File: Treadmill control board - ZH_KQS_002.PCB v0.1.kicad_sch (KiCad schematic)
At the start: 9 parts, among them Q1 IRG4PF50W

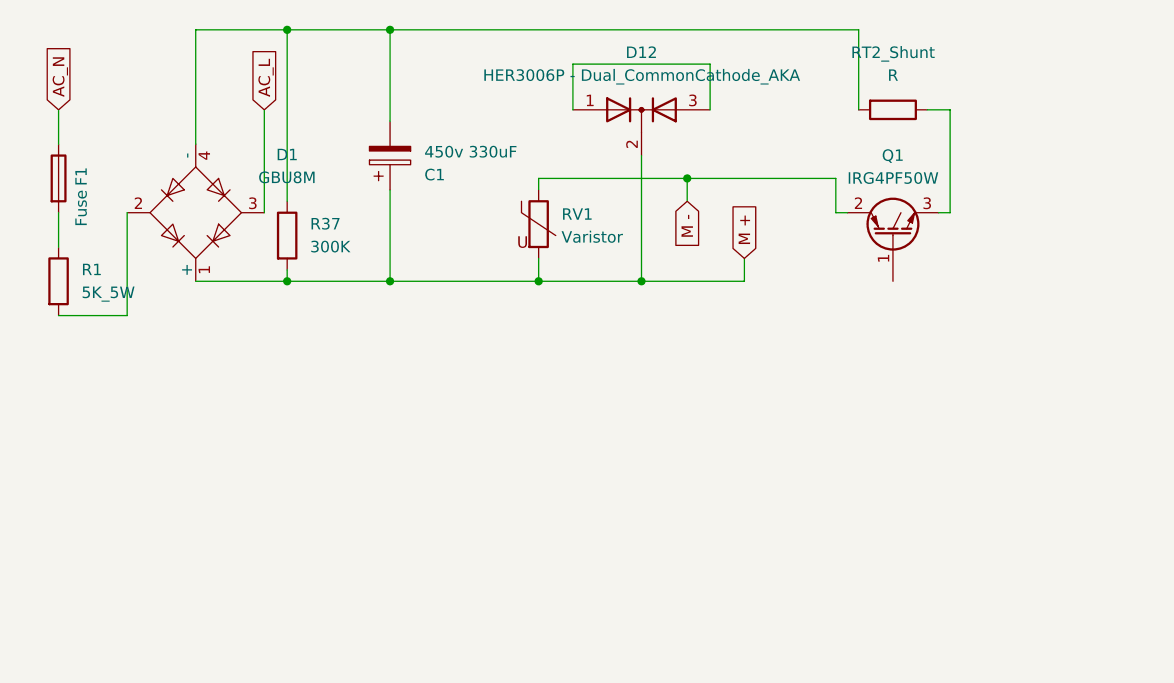
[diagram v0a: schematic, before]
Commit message: Schematic High Voltage side done
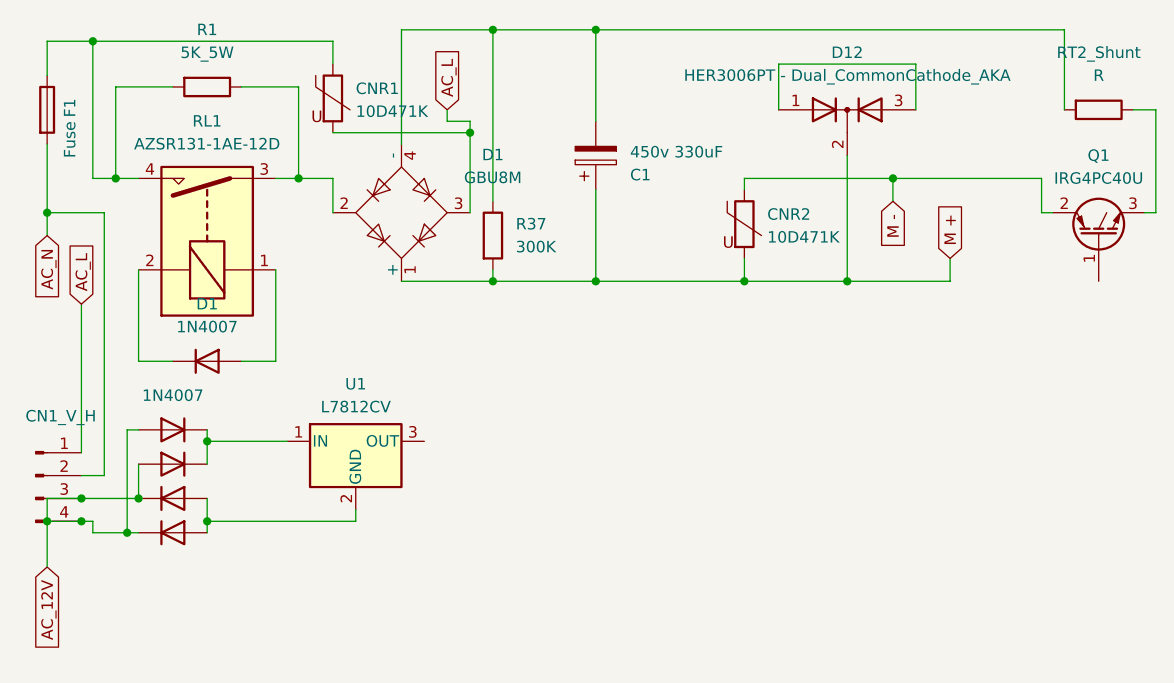
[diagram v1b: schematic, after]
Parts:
- added CN1_V_H: Conn_01x04_Pin, Connector_JST:JST_VH_B4P-VH_1x04_P3.96mm_Vertical, symbol Connector:Conn_01x04_Pin
- added CNR1: 10D471K, Varistor:RV_Disc_D21.5mm_W6.1mm_P7.5mm, symbol Device:Varistor
- added D1, D2, D3, D4, D5: 1N4007, Diode_THT:D_DO-41_SOD81_P10.16mm_Horizontal, symbol Diode:1N4007
- added RL1: AZSR131-1AE-12D, Relay_THT:Relay_SPST_Zettler-AZSR131, symbol Relay:AZSR131-1AE-12D
- added U1: L7812CV, Package_TO_SOT_THT:TO-220-3_Vertical, symbol Regulator_Linear:L7812
- CNR2: renamed from RV1; value Varistor -> 10D471K; footprint (none) -> Varistor:RV_Disc_D21.5mm_W6.1mm_P7.5mm
- D12: value HER3006P - Dual_CommonCathode_AKA -> HER3006PT - Dual_CommonCathode_AKA; footprint (none) -> Package_TO_SOT_THT:TO-247-3_Vertical
- Q1: value IRG4PF50W -> IRG4PC40U
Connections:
- net AC_L: now also CN1_V_H.1 (Pin_1), CNR1.2
- net AC_N: now also F1.2, CN1_V_H.2 (Pin_2); no longer F1.1
- net at R1.2: now also F1.1, CNR1.1, RL1.4; no longer D1.2
- net at R1.1: now also D1.2, RL1.3; no longer F1.2
- new net: D1.1 (K), RL1.2
- new net: D1.2 (A), RL1.1
- new net: D2.1 (K), D3.1 (K), U1.1 (IN)
- new net: D4.2 (A), D5.2 (A), U1.2 (GND)
- new net AC_12V: CN1_V_H.3 (Pin_3), CN1_V_H.4 (Pin_4), D2.2 (A), D3.2 (A), D4.1 (K), D5.1 (K)
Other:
- moved on the sheet: C1, CNR2, D1, D12, F1, Q1, R1, R37, RT2_Shunt

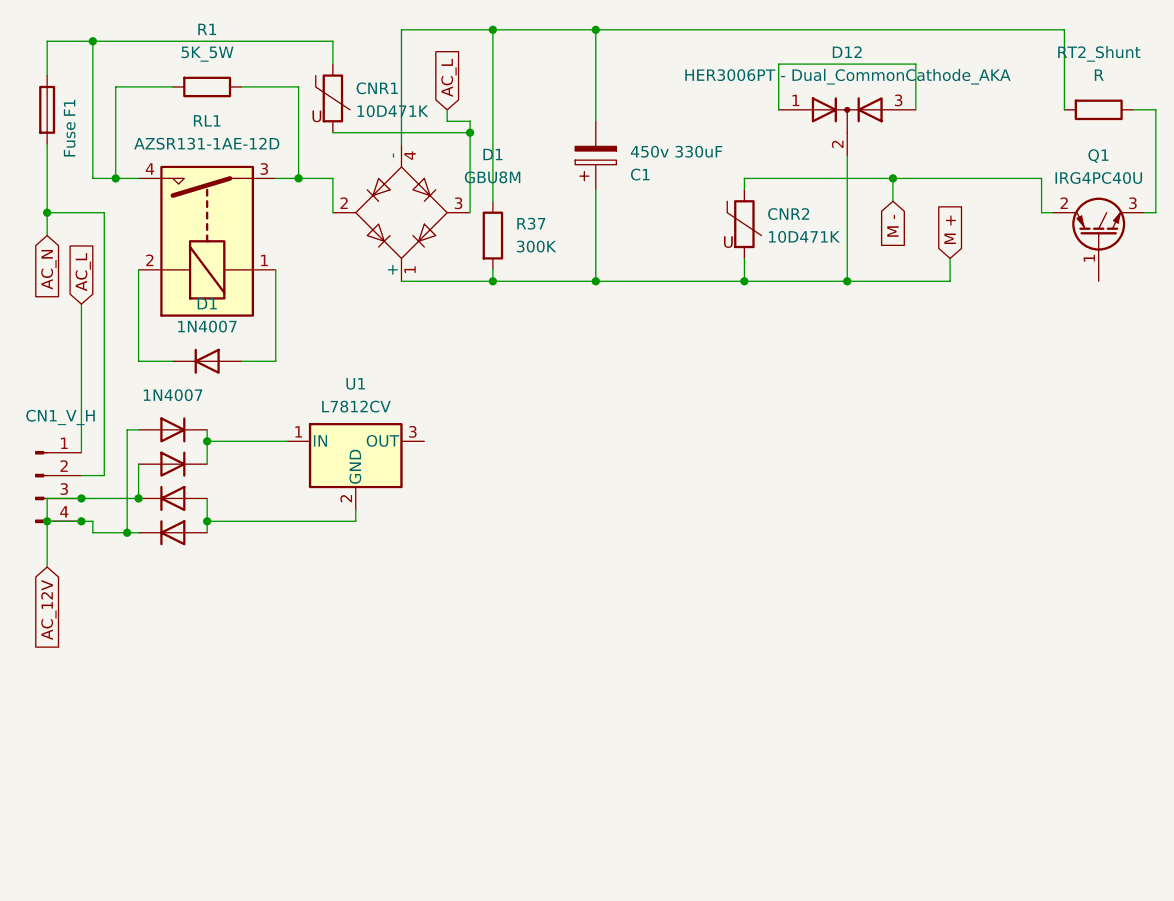
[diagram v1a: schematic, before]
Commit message: Low voltage power supply side done
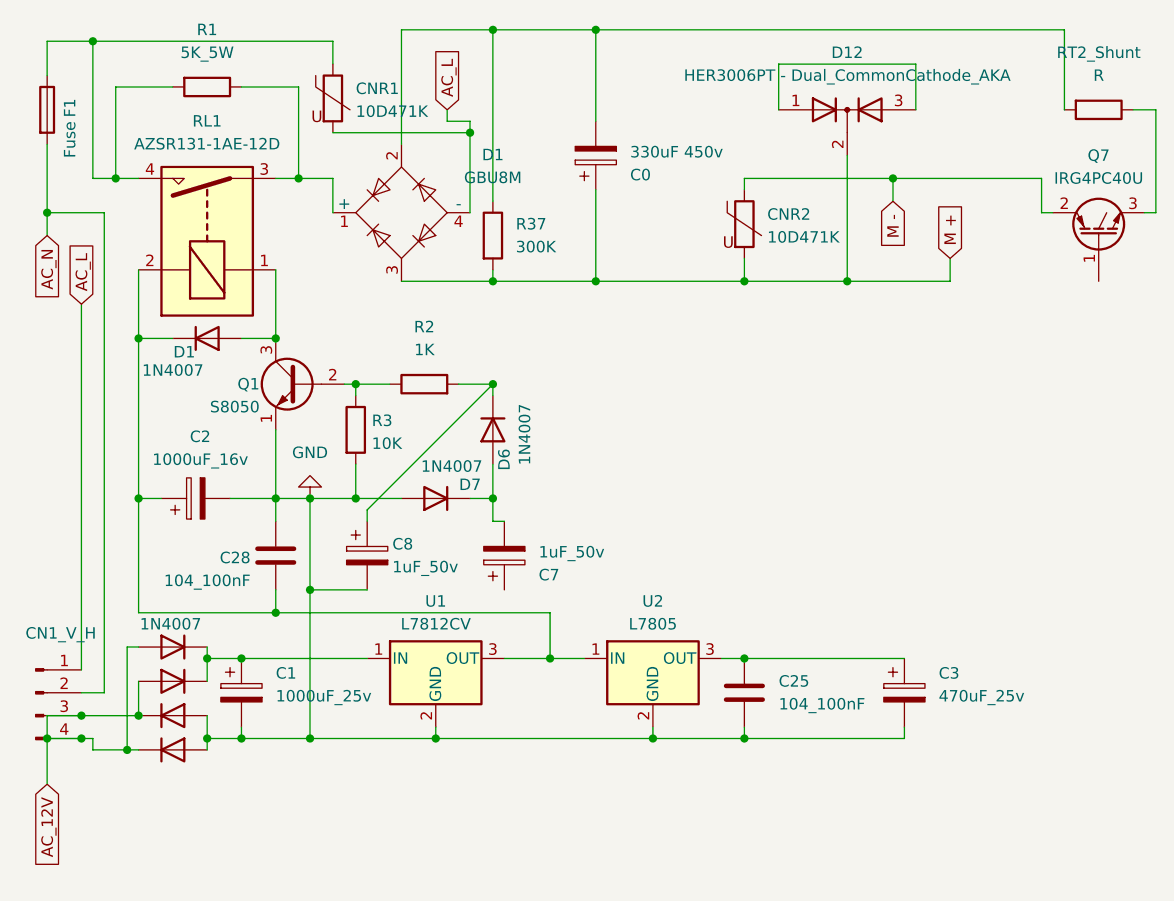
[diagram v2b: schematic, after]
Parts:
- added C1: 1000uF_25v, symbol Device:C_Polarized
- added C2: 1000uF_16v, symbol Device:C_Polarized
- added C25, C28: 104_100nF, symbol Device:C
- added C3: 470uF_25v, symbol Device:C_Polarized
- added C7, C8: 1uF_50v, symbol Device:C_Polarized
- added D6, D7: 1N4007, Diode_THT:D_DO-41_SOD81_P10.16mm_Horizontal, symbol Diode:1N4007
- added Q1: S8050, Package_TO_SOT_THT:TO-92_Inline, symbol Transistor_BJT:S8050
- added R2: 1K, symbol Device:R
- added R3: 10K, symbol Device:R
- added U2: L7805, Package_TO_SOT_THT:TO-220-3_Vertical, symbol Regulator_Linear:L7805
- C0: renamed from C1; value 450v 330uF -> 330uF 450v
- renumbered Q1 to Q7
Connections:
- net AC_L: now also D1.4 (-); no longer D1.3
- net M +: now also D1.3; no longer D1.1 (+)
- net at D1.1 (K), RL1.2: now also U1.3 (OUT), C2.1, C28.2, U2.1 (IN)
- net at D1.2 (A), RL1.1: now also Q1.3 (C)
- net at C0.2, R37.1, RT2_Shunt.2: now also D1.2; no longer D1.4 (-)
- net at D2.1 (K), D3.1 (K), U1.1 (IN): now also C1.1
- net GND: now reaches D4.2 (A), D5.2 (A), U1.2 (GND)
- net GND: now also C1.2, C2.2, C25.2, C28.1, C3.2, C8.2, D7.2 (A), Q1.1 (E), R3.2, U2.2 (GND)
- net at R1.1, RL1.3: now also D1.1 (+); no longer D1.2
- new net: Q1.2 (B), R2.1, R3.1
- new net: C8.1, D6.1 (K), R2.2
- new net: C25.1, C3.1, U2.3 (OUT)
- new net: C7.2, D6.2 (A), D7.1 (K)
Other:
- moved on the sheet: CN1_V_H, D1, U1

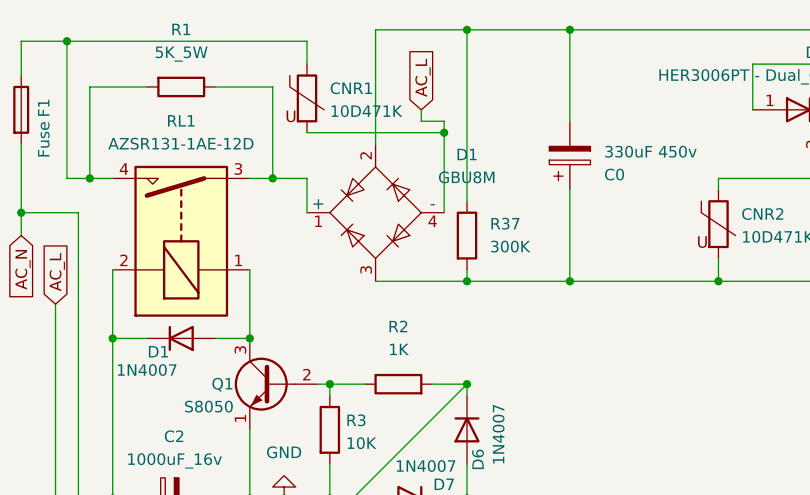
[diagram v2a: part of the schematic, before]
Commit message: Low voltage power supply side done
Low voltage power supply side done and fixed error in Full Bridge Rectifier symbol oriented the wrong way.
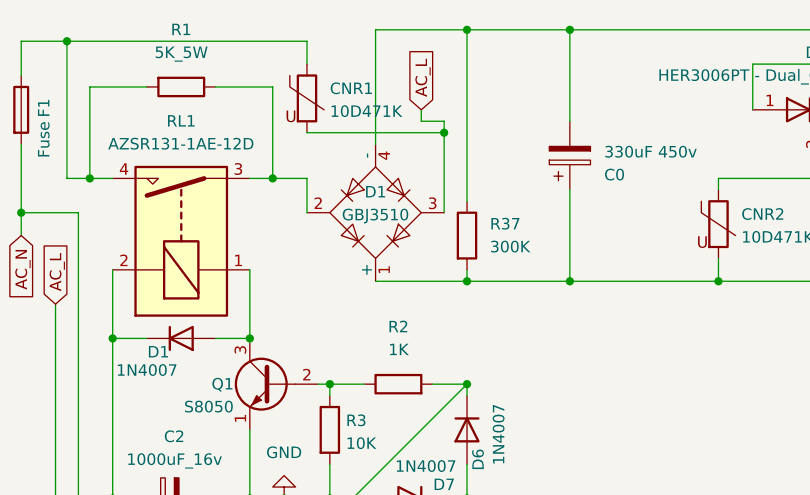
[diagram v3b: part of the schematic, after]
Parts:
- D1: value GBU8M -> GBJ3510
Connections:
- net AC_L: now also D1.3; no longer D1.4 (-)
- net M +: now also D1.1 (+); no longer D1.3
- net at C0.2, R37.1, RT2_Shunt.2: now also D1.4 (-); no longer D1.2
- net at R1.1, RL1.3: now also D1.2; no longer D1.1 (+)
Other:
- moved on the sheet: D1
